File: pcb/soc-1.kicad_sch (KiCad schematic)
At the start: 1 part, among them U1 XC7Z020CLG484

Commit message: hierarchy and cleaning
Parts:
- removed U1: XC7Z020CLG484, Package_BGA:Xilinx_CLG484_CLG485, symbol library:XC7Z020CLG484
- added U1: XC7Z020CLG484, Package_BGA:Xilinx_CLG484_CLG485, symbol library:XC7Z020CLG484
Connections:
- new net CAM0_0_N: U1.V9 (IO_L1N_T0_13)
- new net CAM0_0_P: U1.V10 (IO_L1P_T0_13)
- new net CAM0_1_N: U1.W8 (IO_L2N_T0_13)
- new net CAM0_1_P: U1.V8 (IO_L2P_T0_13)
- new net CAM0_2_N: U1.W10 (IO_L3N_T0_DQS_13)
- new net CAM0_2_P: U1.W11 (IO_L3P_T0_DQS_13)

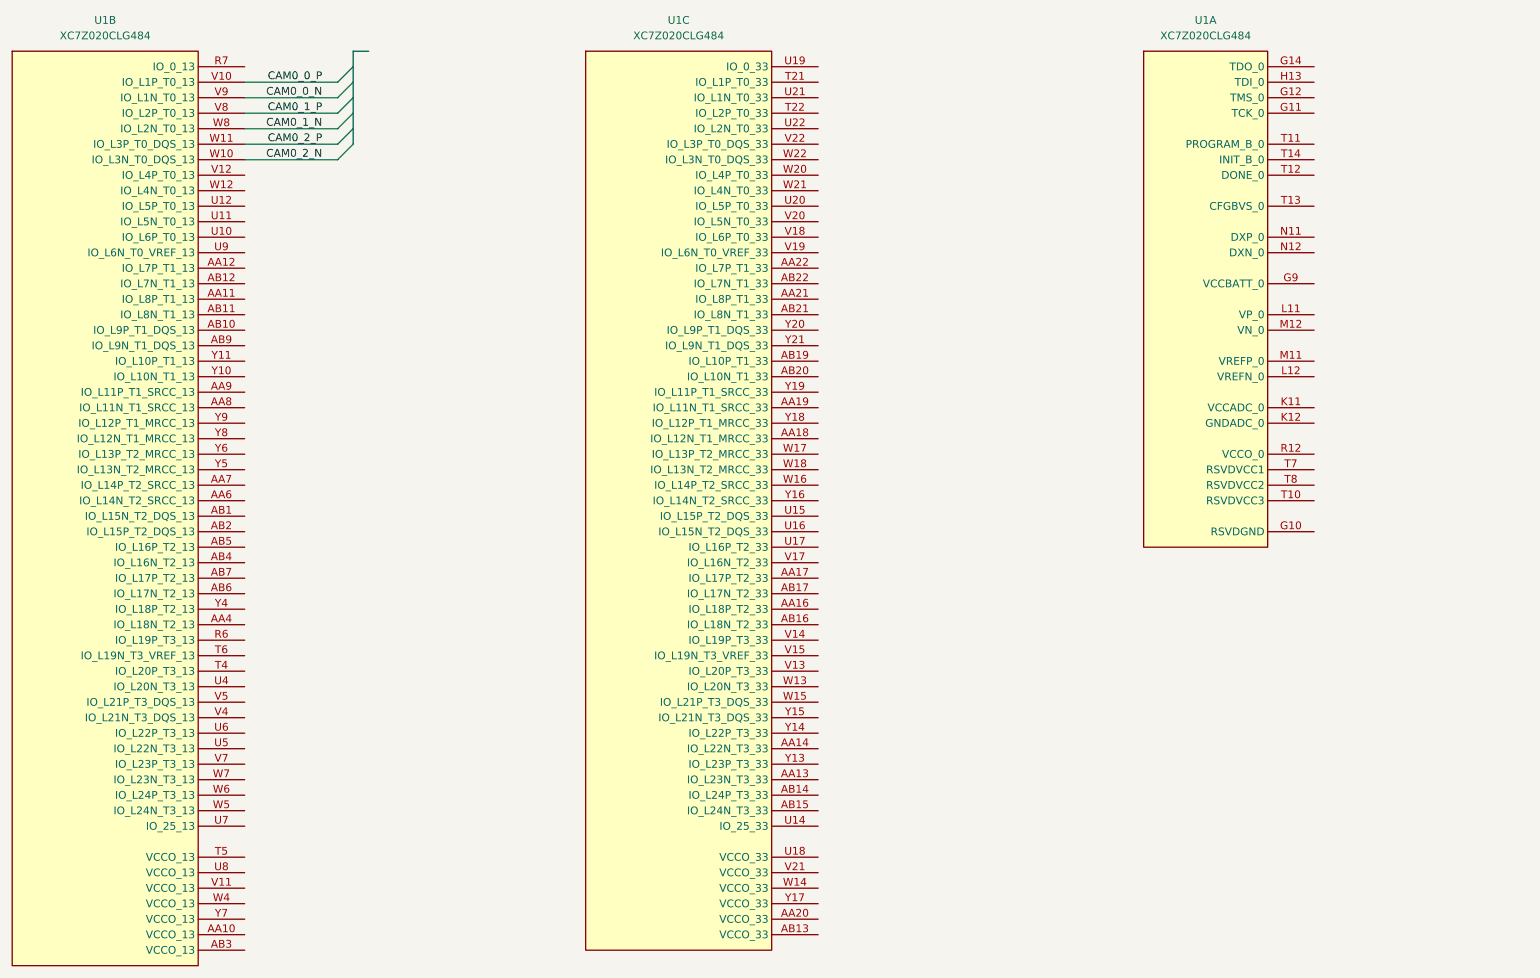
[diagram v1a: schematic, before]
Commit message: schematic structure, added qspi flash, pinout defs. mostly work on PS pinouts, defining comms. buses, still need to choose dram part, phys, camera/bus, power supply etc
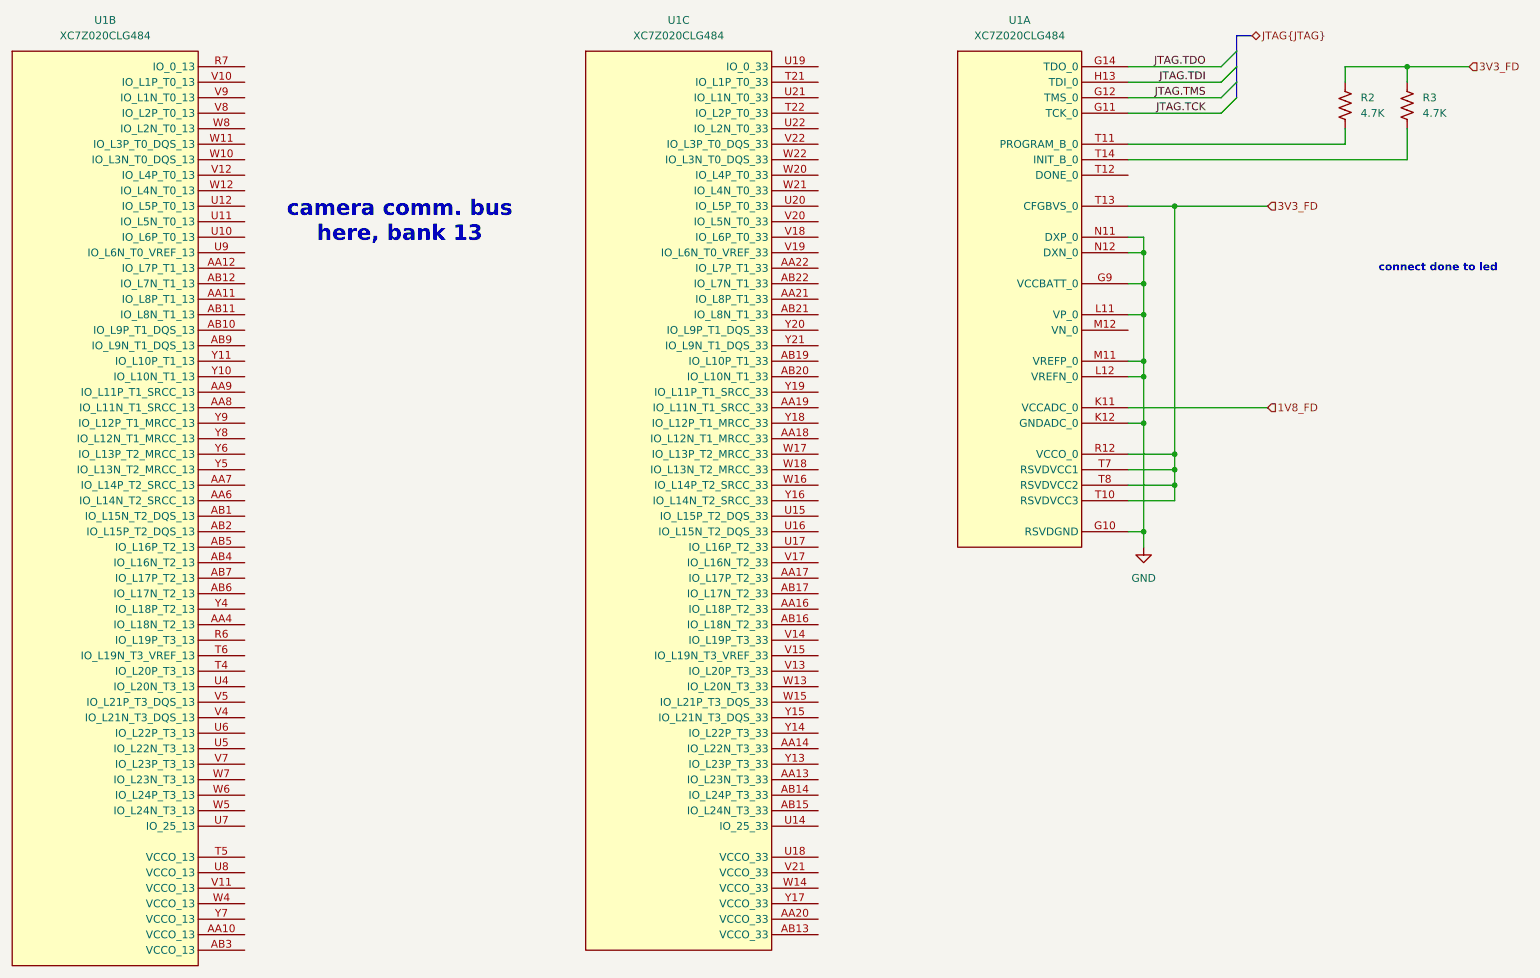
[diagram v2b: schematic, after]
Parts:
- added R2, R3: 4.7K, Resistor_SMD:R_0402_1005Metric, symbol Device:R_US
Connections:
- net GND: now reaches U1.G10 (RSVDGND)
- net GND: now also U1.G9 (VCCBATT_0), U1.K12 (GNDADC_0), U1.L11 (VP_0), U1.L12 (VREFN_0), U1.M11 (VREFP_0), U1.N11 (DXP_0), U1.N12 (DXN_0)
- net JTAG.TCK: now reaches U1.G11 (TCK_0)
- net JTAG.TMS: now reaches U1.G12 (TMS_0)
- net JTAG.TDO: now reaches U1.G14 (TDO_0)
- net JTAG.TDI: now reaches U1.H13 (TDI_0)
- net 1V8_FD: now reaches U1.K11 (VCCADC_0)
- net 3V3_FD: now reaches U1.R12 (VCCO_0)
- net 3V3_FD: now also U1.T10 (RSVDVCC3), U1.T13 (CFGBVS_0), U1.T7 (RSVDVCC1), U1.T8 (RSVDVCC2), R2.1, R3.1
- net at U1.T11 (PROGRAM_B_0): now also R2.2
- net at U1.T14 (INIT_B_0): now also R3.2
- net CAM0_0_N: no longer names the net of U1.V9 (IO_L1N_T0_13)
- net CAM0_0_P: no longer names the net of U1.V10 (IO_L1P_T0_13)
- net CAM0_1_N: no longer names the net of U1.W8 (IO_L2N_T0_13)
- net CAM0_1_P: no longer names the net of U1.V8 (IO_L2P_T0_13)
- net CAM0_2_N: no longer names the net of U1.W10 (IO_L3N_T0_DQS_13)
- net CAM0_2_P: no longer names the net of U1.W11 (IO_L3P_T0_DQS_13)
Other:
- note added: "camera comm. bus here, bank 13"
- note added: "connect done to led"
- title: (none) -> CUTIE-CITRUS
- moved on the sheet: U1A

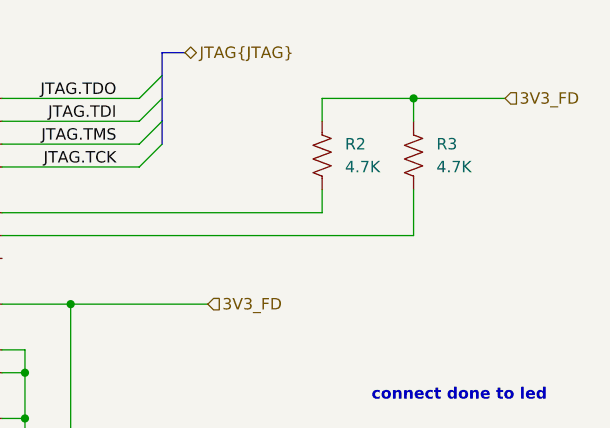
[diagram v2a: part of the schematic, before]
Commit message: added ddr3l
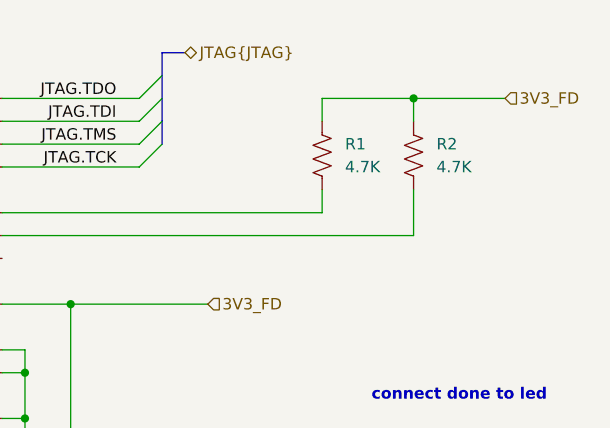
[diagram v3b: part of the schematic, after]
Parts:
- renumbered R2 to R1, R3 to R2
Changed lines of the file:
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@@
 		(dnp no)
 		(fields_autoplaced yes)
-		(property "Reference" "R3"
+		(property "Reference" "R2"
 			(at 251.46 33.0199 0)
 			(effects
@@
 			(project "CUTIE-CITRUS"
 				(path "/875da261-7543-41df-9bd5-25bca104c872/ed92714e-f3d1-4199-bde0-4965b17657c9/73a27263-8599-464b-937c-871c9e5b89cb"
-					(reference "R3")
+					(reference "R2")
 					(unit 1)
 				)
@@
 		(dnp no)
 		(fields_autoplaced yes)
-		(property "Reference" "R2"
+		(property "Reference" "R1"
 			(at 241.3 33.0199 0)
 			(effects
@@
 			(project "CUTIE-CITRUS"
 				(path "/875da261-7543-41df-9bd5-25bca104c872/ed92714e-f3d1-4199-bde0-4965b17657c9/73a27263-8599-464b-937c-871c9e5b89cb"
-					(reference "R2")
+					(reference "R1")
 					(unit 1)
 				)
@@
 		(dnp no)
 		(fields_autoplaced yes)
-		(property "Reference" "#PWR03"
+		(property "Reference" "#PWR01"
 			(at 205.74 113.03 0)
 			(effects
@@
 			(project ""
 				(path "/875da261-7543-41df-9bd5-25bca104c872/ed92714e-f3d1-4199-bde0-4965b17657c9/73a27263-8599-464b-937c-871c9e5b89cb"
-					(reference "#PWR03")
+					(reference "#PWR01")
 					(unit 1)
 				)
